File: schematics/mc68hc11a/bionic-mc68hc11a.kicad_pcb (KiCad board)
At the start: 2 copper layers, 27.9 x 68.6 mm, 8 parts, among them J1 Bionic-P135, J2 Bionic-P245, U1 MC68HC11A0P, U2 11AA010-I/TT

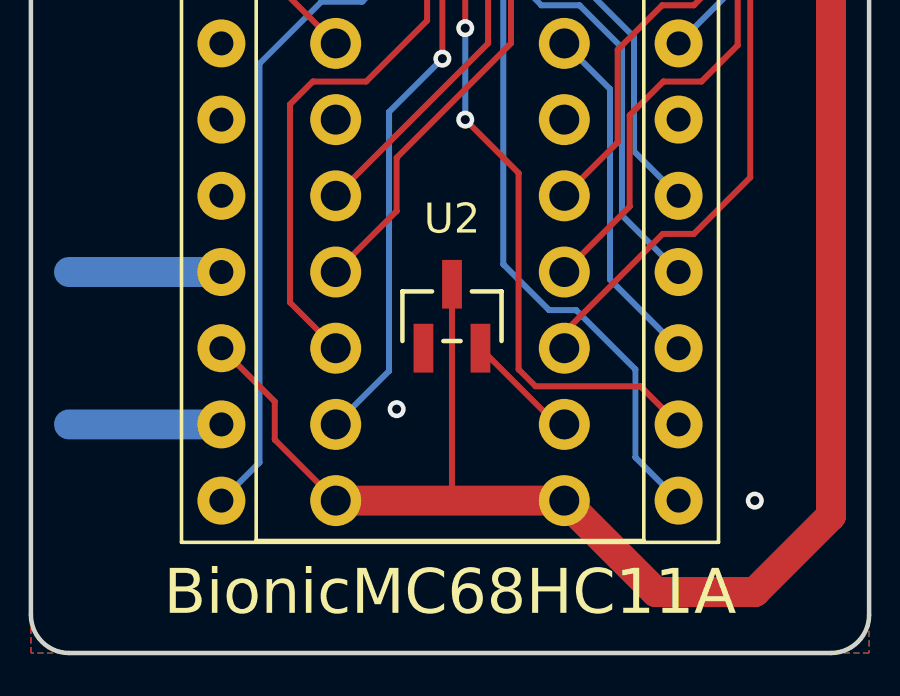
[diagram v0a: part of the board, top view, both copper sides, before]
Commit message: [MC68HC11A] Fix EEPROM pinout
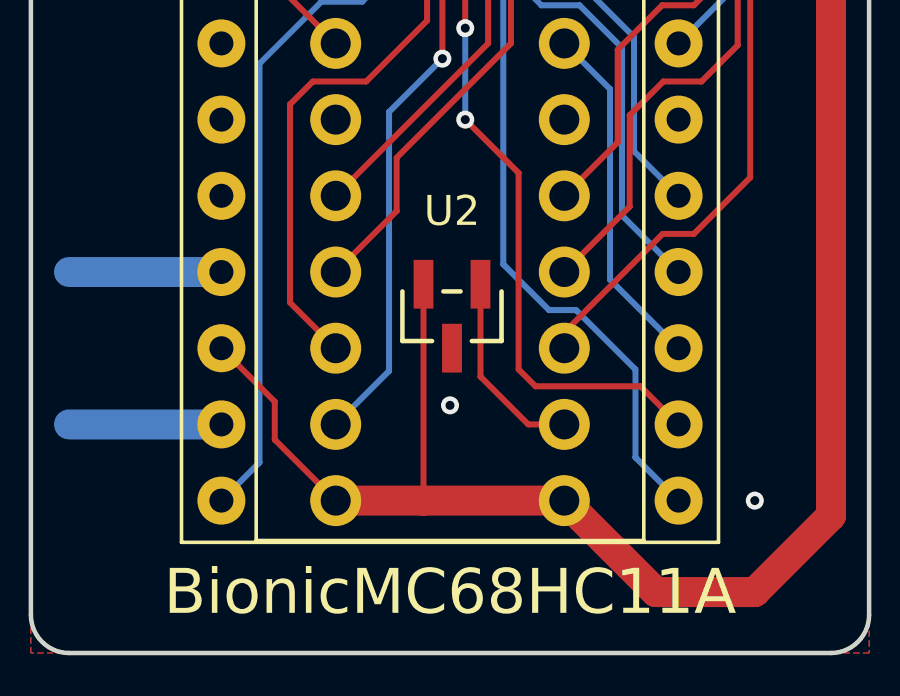
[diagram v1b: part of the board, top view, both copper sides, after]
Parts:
- turned U2 to 180 degrees
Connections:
- U2 pad 1: GND -> /P57
- U2 pad 2: /P57 -> VCC
- U2 pad 3: VCC -> GND
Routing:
- net /P57: track 3.85 -> 6.53 mm
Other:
- board text added: "Rev. 4"
- board text removed: "Rev. 3"
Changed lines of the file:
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@@
   (title_block
     (title "BionicMC68HC11A")
-    (date "2024-03-27")
-    (rev "2")
+    (date "2024-11-01")
+    (rev "4")
     (company "Tadashi G. Takaoka")
   )
@@
   )
   (footprint "0-LocalLibrary:SOT-23_MC_MCH-M" (layer "F.Cu")
-    (at 115.036 127.354)
+    (at 115.035999 127.354 180)
     (tags "11aa010t-i/tt ")
     (property "Sheetfile" "bionic-mc68hc11a.kicad_sch")
@@
     (property "ki_keywords" "11AA010-I")
     (attr smd)
-    (fp_text reference "U2" (at 0 -3.252 unlocked) (layer "F.SilkS")
+    (fp_text reference "U2" (at 0 3.506 unlocked) (layer "F.SilkS")
         (effects (font (size 1 1) (thickness 0.15)))
     )
-    (fp_text value "11AA010-I/TT" (at 0 0 unlocked) (layer "F.Fab")
+    (fp_text value "11AA010-I/TT" (at 0 0 180 unlocked) (layer "F.Fab")
         (effects (font (size 1 1) (thickness 0.15)))
     )
-    (fp_text user "${REFERENCE}" (at 0 0 unlocked) (layer "F.Fab")
+    (fp_text user "${REFERENCE}" (at 0 0 180 unlocked) (layer "F.Fab")
         (effects (font (size 1 1) (thickness 0.15)))
     )
@@
     (fp_circle (center -1.270999 0.446) (end -1.143999 0.446)
       (stroke (width 0.0254) (type solid)) (fill none) (layer "F.Fab"))
-    (pad "1" smd rect (at -0.950001 1.066) (size 0.6604 1.6256) (layers "F.Cu" "F.Paste" "F.Mask")
+    (pad "1" smd rect (at -0.950001 1.066 180) (size 0.6604 1.6256) (layers "F.Cu" "F.Paste" "F.Mask")
+      (net 25 "/P57") (pinfunction "SCIO") (pintype "bidirectional"))
+    (pad "2" smd rect (at 0.950001 1.066 180) (size 0.6604 1.6256) (layers "F.Cu" "F.Paste" "F.Mask")
+      (net 1 "VCC") (pinfunction "VCC") (pintype "power_in"))
+    (pad "3" smd rect (at 0 -1.066 180) (size 0.6604 1.6256) (layers "F.Cu" "F.Paste" "F.Mask")
       (net 2 "GND") (pinfunction "VSS") (pintype "power_in"))
-    (pad "2" smd rect (at 0.950001 1.066) (size 0.6604 1.6256) (layers "F.Cu" "F.Paste" "F.Mask")
-      (net 25 "/P57") (pinfunction "SCIO") (pintype "bidirectional"))
-    (pad "3" smd rect (at 0 -1.066) (size 0.6604 1.6256) (layers "F.Cu" "F.Paste" "F.Mask")
-      (net 1 "VCC") (pinfunction "VCC") (pintype "power_in"))
     (model "${KIPRJMOD}/0-LocalLibrary/SOT-23_MC_MCH.step"
       (offset (xyz 0 0 0))
@@
     (effects (font (size 0.8 0.8)) (justify bottom mirror))
   )
-  (gr_text "Rev. 3" (at 106.842 136.802) (layer "B.SilkS")
+  (gr_text "Rev. 4" (at 106.842 136.802) (layer "B.SilkS")
     (effects (font (size 1 1)) (justify left mirror))
   )
@@
   (segment locked (start 125.13 136.548) (end 127.67 134.008) (width 1) (layer "F.Cu") (net 1))
   (segment locked (start 126.654 75.08) (end 122.59 75.08) (width 1) (layer "F.Cu") (net 1))
-  (segment (start 115.036 126.288) (end 115.036 133.5) (width 0.2) (layer "F.Cu") (net 1))
   (segment locked (start 121.828 136.548) (end 125.13 136.548) (width 1) (layer "F.Cu") (net 1))
+  (segment (start 114.081 133.5) (end 118.78 133.5) (width 1) (layer "F.Cu") (net 1))
+  (segment (start 114.085998 126.288) (end 114.085998 133.495002) (width 0.2) (layer "F.Cu") (net 1))
   (segment (start 109.128 131.468) (end 111.16 133.5) (width 0.2) (layer "F.Cu") (net 1))
   (segment (start 109.128 130.198) (end 109.128 131.468) (width 0.2) (layer "F.Cu") (net 1))
+  (segment (start 111.16 133.5) (end 114.081 133.5) (width 1) (layer "F.Cu") (net 1))
   (segment (start 119.288 71.778) (end 122.59 75.08) (width 0.2) (layer "F.Cu") (net 1))
   (segment (start 107.35 128.42) (end 109.128 130.198) (width 0.2) (layer "F.Cu") (net 1))
@@
   (segment locked (start 127.67 76.096) (end 126.654 75.08) (width 1) (layer "F.Cu") (net 1))
   (segment locked (start 118.78 133.5) (end 121.828 136.548) (width 1) (layer "F.Cu") (net 1))
-  (segment locked (start 111.16 133.5) (end 118.78 133.5) (width 1) (layer "F.Cu") (net 1))
+  (segment (start 114.085998 133.495002) (end 114.081 133.5) (width 0.2) (layer "F.Cu") (net 1))
   (segment (start 126.908 75.334) (end 126.908 74.9265) (width 0.2) (layer "F.Cu") (net 1))
   (segment (start 110.906 133.5) (end 111.16 133.5) (width 0.2) (layer "F.Cu") (net 1))
   (segment (start 115.7447 71.778) (end 119.288 71.778) (width 0.2) (layer "F.Cu") (net 1))
-  (via (at 113.192 130.452) (size 0.6) (drill 0.3) (layers "F.Cu" "B.Cu") (free) (net 2))
+  (via (at 114.97 130.325) (size 0.6) (drill 0.3) (layers "F.Cu" "B.Cu") (free) (net 2))
   (via (at 125.13 133.5) (size 0.6) (drill 0.3) (layers "F.Cu" "B.Cu") (free) (net 2))
   (segment (start 107.35 125.88) (end 102.27 125.88) (width 1) (layer "B.Cu") (net 2))
@@
   (segment (start 112.938 120.546) (end 112.938 129.182) (width 0.2) (layer "B.Cu") (net 24))
   (segment (start 122.5286 98.0014) (end 122.59 97.94) (width 0.2) (layer "B.Cu") (net 24))
-  (segment (start 115.986 128.42) (end 118.526 130.96) (width 0.2) (layer "F.Cu") (net 25))
-  (segment (start 118.526 130.96) (end 118.78 130.96) (width 0.2) (layer "F.Cu") (net 25))
+  (segment (start 115.986 126.288) (end 115.986 129.368081) (width 0.2) (layer "F.Cu") (net 25))
+  (segment (start 117.577919 130.96) (end 118.78 130.96) (width 0.2) (layer "F.Cu") (net 25))
+  (segment (start 115.986 129.368081) (end 117.577919 130.96) (width 0.2) (layer "F.Cu") (net 25))
   (segment (start 120.304 126.134) (end 122.59 128.42) (width 0.2) (layer "B.Cu") (net 27))
   (segment (start 120.304 119.784) (end 120.304 126.134) (width 0.2) (layer "B.Cu") (net 27))

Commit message: [MC68HC11A] Shrink board size
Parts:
- C2: moved to B.Cu
- moved C2 3.05 mm to (123.9, 74.2)
- moved C1 1.28 mm to (123.9, 74.2)
- moved U2 1.27 mm to (113.8, 127.4)
- moved D1 1.27 mm to (113.7, 71.8)
- moved J1 1.27 mm to (109.9, 75.1)
- moved J2 1.27 mm to (117.5, 75.1)
- moved R1 1.27 mm to (109.9, 71.8)
- moved U1 1.27 mm to (106.1, 75.1)
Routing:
- net GND: track 10.2 -> 2.92 mm, vias 2 -> 19
- net /P54: track 44.1 -> 45.8 mm
- net /P56: track 55.0 -> 56.6 mm
- net /P12: track 41.0 -> 42.5 mm
- net /P55: track 49.7 -> 51.2 mm
- net /P10: track 55.8 -> 57.3 mm
- net /P42: track 33.7 -> 34.8 mm
- net /P43: track 31.8 -> 30.9 mm
- net /P57: track 6.53 -> 5.83 mm
- net /P40: track 37.6 -> 36.9 mm
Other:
- board size 27.9 x 68.6 mm -> 25.4 x 68.6 mm

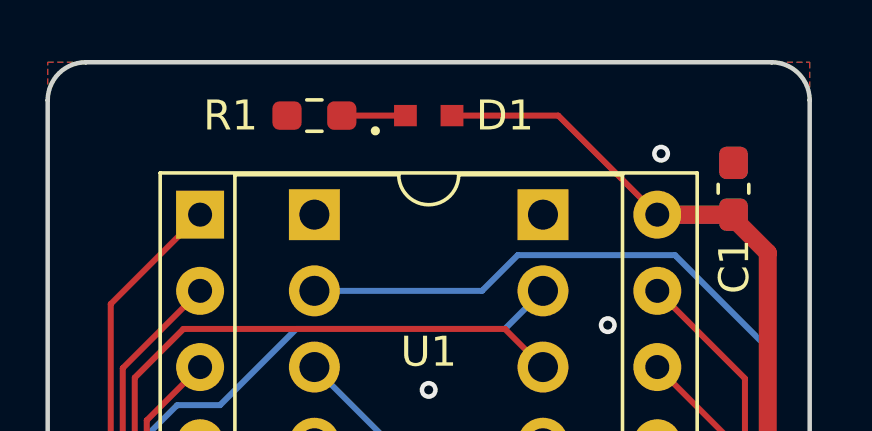
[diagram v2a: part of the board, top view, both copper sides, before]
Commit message: [schematics] Update LED footprint
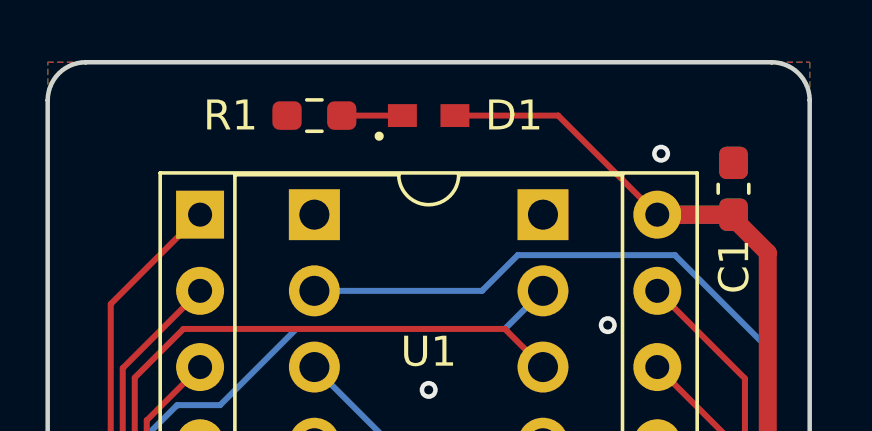
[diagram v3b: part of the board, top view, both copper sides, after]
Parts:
- D1: footprint 0-LocalLibrary:LED_CSL1901UW1_ROM -> 0-LocalLibrary:LED_CSL1901UW1_ROM-M

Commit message: [MC68HC11A] Cleanup schematics
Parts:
- D1: footprint 0-LocalLibrary:LED_CSL1901UW1_ROM-M -> rhom:LED_CSL1901UW1_ROM-M
- J1: footprint 0-LocalLibrary:Bionic-P135_Vertical -> bionic:Bionic-P135_Vertical
- J2: footprint 0-LocalLibrary:Bionic-P245_Vertical -> bionic:Bionic-P245_Vertical
- U1: footprint 0-LocalLibrary:DIP-48_W15.24mm_Socket -> bionic:DIP-48_W15.24mm_Socket
- U2: footprint 0-LocalLibrary:SOT-23_MC_MCH-M -> microchip:SOT-23_MC_MCH-M
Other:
- rule pad_to_mask_clearance: 0.051 -> 0
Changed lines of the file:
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@@
 			(dielectric_constraints no)
 		)
-		(pad_to_mask_clearance 0.051)
-		(solder_mask_min_width 0.25)
+		(pad_to_mask_clearance 0)
 		(allow_soldermask_bridges_in_footprints no)
 		(aux_axis_origin 101 70)
@@
 		)
 	)
-	(footprint "0-LocalLibrary:DIP-48_W15.24mm_Socket"
+	(footprint "bionic:DIP-48_W15.24mm_Socket"
 		(layer "F.Cu")
 		(at 106.08 75.08)
@@
 		(tags "THT DIP DIL PDIP 2.54mm 15.24mm 600mil Socket")
 		(property "Reference" "U1"
-			(at 7.62 4.572 0)
+			(at 7.62 4.3688 0)
 			(layer "F.SilkS")
 			(effects
@@
 			)
 		)
-		(property "Footprint" "0-LocalLibrary:DIP-48_W15.24mm_Socket"
+		(property "Footprint" "bionic:DIP-48_W15.24mm_Socket"
 			(at 0 0 0)
 			(layer "F.Fab")
@@
 			)
 		)
-		(property "Description" ""
+		(property "Description" "8-bit General Purpose Microprocessor, DIP-48"
 			(at 0 0 0)
 			(layer "F.Fab")
@@
 		)
 	)
-	(footprint "0-LocalLibrary:SOT-23_MC_MCH-M"
+	(footprint "microchip:SOT-23_MC_MCH-M"
 		(layer "F.Cu")
 		(at 113.765999 127.354 180)
-		(tags "11aa010t-i/tt ")
+		(descr "Microchip 11AAxxx-I/TT UNI/O 1Kbit Serial EEPROM")
 		(property "Reference" "U2"
-			(at 0 3.506 0)
+			(at 0 3.1504 0)
 			(unlocked yes)
 			(layer "F.SilkS")
@@
 			)
 		)
-		(property "Footprint" "0-LocalLibrary:SOT-23_MC_MCH-M"
+		(property "Footprint" "microchip:SOT-23_MC_MCH-M"
 			(at 0 0 180)
 			(layer "F.Fab")
@@
 			)
 		)
-		(property "Description" ""
+		(property "Description" "UNI/O Serial EEPROM (1Kbit)"
 			(at 0 0 180)
 			(layer "F.Fab")
@@
 			(pintype "power_in")
 		)
-		(model "${KIPRJMOD}/0-LocalLibrary/SOT-23_MC_MCH.step"
+		(model "${KIPRJMOD}/microchip.pretty/SOT-23_MC_MCH.step"
 			(offset
 				(xyz 0 0 0)
@@
 		)
 	)
-	(footprint "0-LocalLibrary:LED_CSL1901UW1_ROM-M"
+	(footprint "rhom:LED_CSL1901UW1_ROM-M"
 		(layer "F.Cu")
 		(at 113.7 71.778)
@@
 		(tags "CSL1901UW1 ")
 		(property "Reference" "D1"
-			(at 2.8448 0 0)
+			(at 2.9464 0 0)
 			(unlocked yes)
 			(layer "F.SilkS")
@@
 			)
 		)
-		(property "Footprint" "0-LocalLibrary:LED_CSL1901UW1_ROM-M"
+		(property "Footprint" "rhom:LED_CSL1901UW1_ROM-M"
 			(at 0 0 0)
 			(layer "F.Fab")
@@
 			)
 		)
-		(property "Description" ""
+		(property "Description" "Red LED (Low Current Emission, SMD)"
 			(at 0 0 0)
 			(layer "F.Fab")
@@
 			)
 		)
+		(model "${KIPRJMOD}/rhom.pretty/LED_CSL1901UW1_ROM.step"
+			(offset
+				(xyz 0 0 0)
+			)
+			(scale
+				(xyz 1 1 1)
+			)
+			(rotate
+				(xyz 0 0 0)
+			)
+		)
 	)
-	(footprint "0-LocalLibrary:Bionic-P245_Vertical"
+	(footprint "bionic:Bionic-P245_Vertical"
 		(layer "B.Cu")
 		(at 117.51 75.08 180)
@@
 			)
 		)
-		(property "Footprint" "0-LocalLibrary:Bionic-P245_Vertical"
-			(at 0 0 180)
-			(layer "F.Fab")
+		(property "Footprint" "bionic:Bionic-P245_Vertical"
+			(at 0 0 0)
+			(layer "B.Fab")
 			(hide yes)
 			(effects
@@
 					(thickness 0.15)
 				)
+				(justify mirror)
 			)
 		)
 		(property "Datasheet" ""
-			(at 0 0 180)
-			(layer "F.Fab")
+			(at 0 0 0)
+			(layer "B.Fab")
 			(hide yes)
 			(effects
@@
 					(thickness 0.15)
 				)
-			)
-		)
-		(property "Description" ""
-			(at 0 0 180)
-			(layer "F.Fab")
+				(justify mirror)
+			)
+		)
+		(property "Description" "Generic connector, single row, 01x24, script generated (kicad-library-utils/schlib/autogen/connector/)"
+			(at 0 0 0)
+			(layer "B.Fab")
 			(hide yes)
 			(effects
@@
 					(thickness 0.15)
 				)
+				(justify mirror)
 			)
 		)
@@
 		)
 	)
-	(footprint "0-LocalLibrary:Bionic-P135_Vertical"
+	(footprint "bionic:Bionic-P135_Vertical"
 		(layer "B.Cu")
 		(at 109.89 75.08 180)
@@
 			)
 		)
-		(property "Footprint" "0-LocalLibrary:Bionic-P135_Vertical"
-			(at 0 0 180)
-			(layer "F.Fab")
+		(property "Footprint" "bionic:Bionic-P135_Vertical"
+			(at 0 0 0)
+			(layer "B.Fab")
 			(hide yes)
 			(effects
@@
 					(thickness 0.15)
 				)
+				(justify mirror)
 			)
 		)
 		(property "Datasheet" ""
-			(at 0 0 180)
-			(layer "F.Fab")
+			(at 0 0 0)
+			(layer "B.Fab")
 			(hide yes)
 			(effects
@@
 					(thickness 0.15)
 				)
-			)
-		)
-		(property "Description" ""
-			(at 0 0 180)
-			(layer "F.Fab")
+				(justify mirror)
+			)
+		)
+		(property "Description" "Generic connector, single row, 01x24, script generated (kicad-library-utils/schlib/autogen/connector/)"
+			(at 0 0 0)
+			(layer "B.Fab")
 			(hide yes)
 			(effects
@@
 					(thickness 0.15)
 				)
-			)
-		)
+				(justify mirror)
+			)
+		)

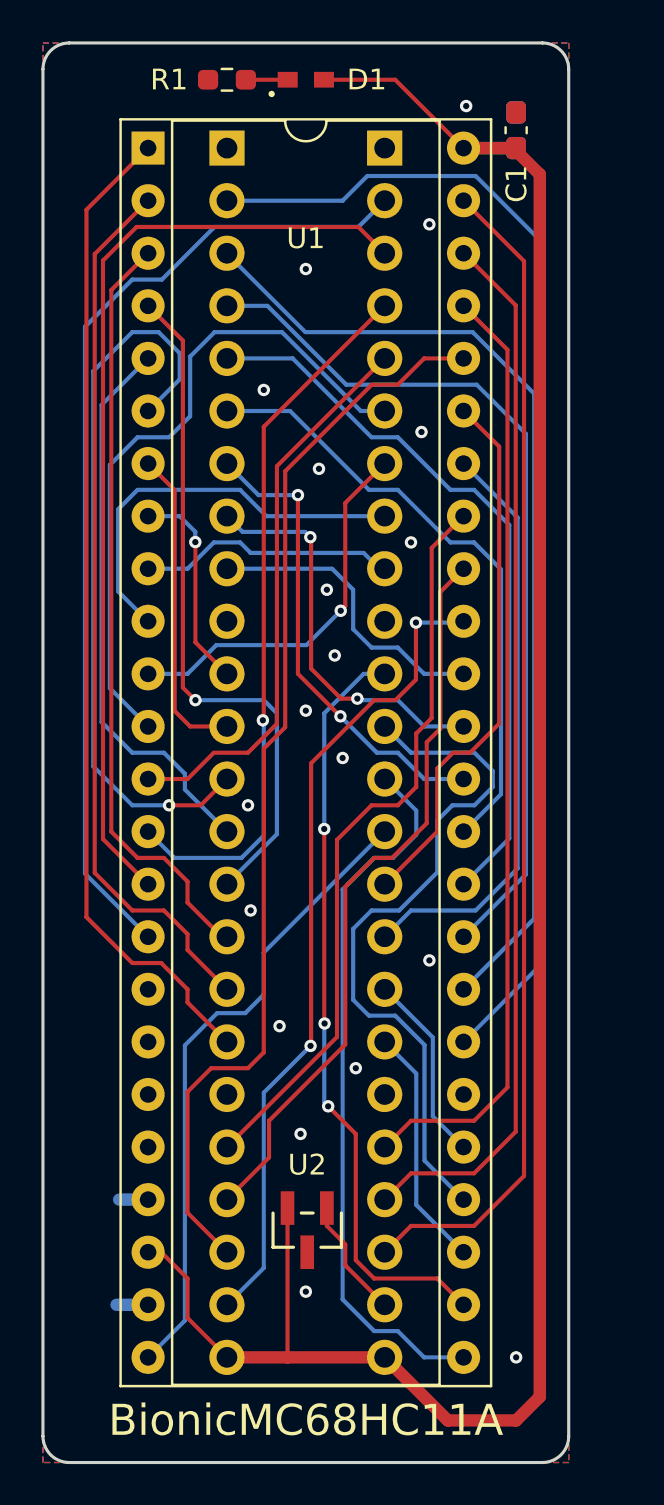
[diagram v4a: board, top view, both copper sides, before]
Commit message: [MC68HC11A] Update schematics
Remove unused pins from bionic connector
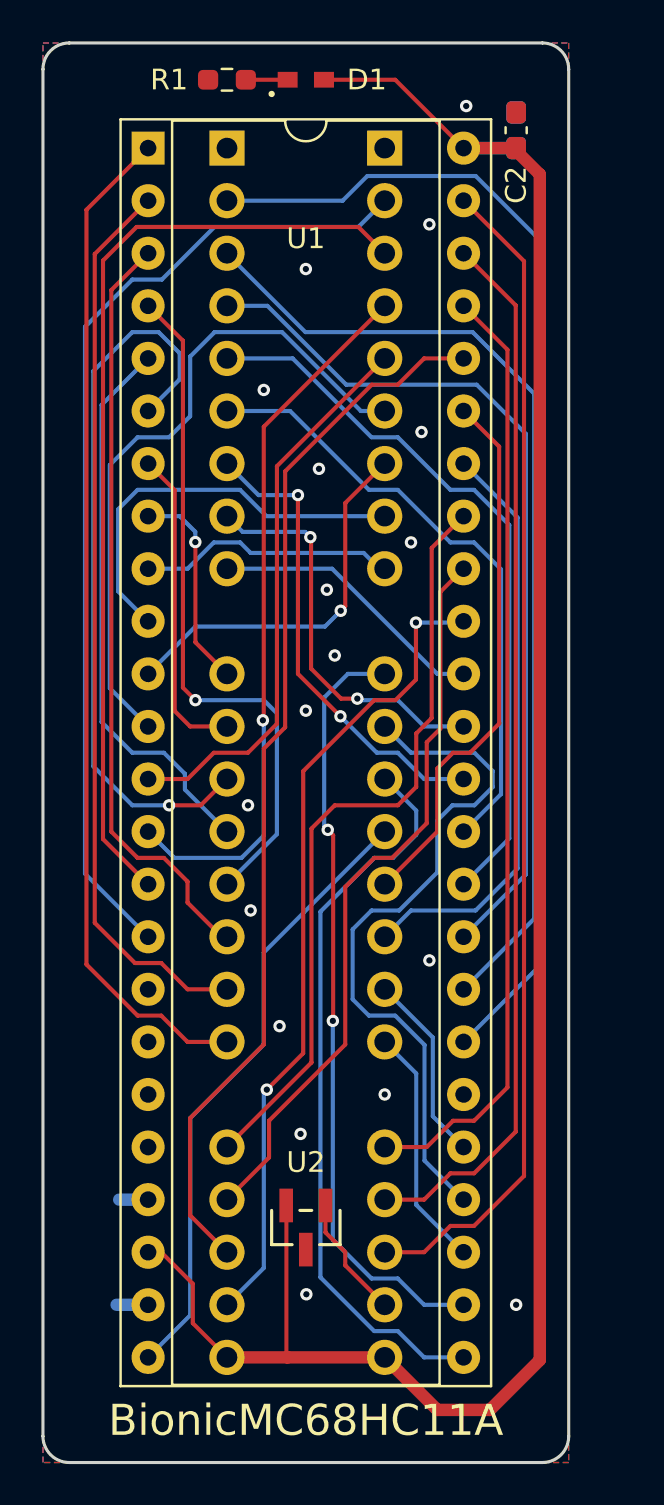
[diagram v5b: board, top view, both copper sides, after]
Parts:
- C1: moved to B.Cu
- C2: moved to F.Cu
- J1: footprint bionic:Bionic-P135_Vertical -> bionic:Bionic-P135_THT
- J2: footprint bionic:Bionic-P245_Vertical -> bionic:Bionic-P245_THT
- moved U2 0.14 mm to (113.7, 127.2)
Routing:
- net VCC: track 105.5 -> 104.2 mm
- net /P52: track 52.4 -> 51.2 mm
- net /P17: track 14.7 -> 13.5 mm
- net /P50: track 36.0 -> 37.0 mm
- net /P36: track 42.7 -> 43.7 mm
- net /P37: track 48.0 -> 49.0 mm
- net /P42: track 34.8 -> 35.7 mm
- net /P43: track 30.9 -> 30.1 mm
- net /P40: track 36.9 -> 37.4 mm, vias 3 -> 2
- net GND: vias 19 -> 18
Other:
- board text added: "Rev. 5"
- board text removed: "Rev. 4"
